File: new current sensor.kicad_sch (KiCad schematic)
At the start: 51 parts, among them J1 Conn_01x04, U1 ACS711xEXLT-31AB, U2 ACS711xEXLT-31AB, U3 ACS711xEXLT-31AB, U4 ACS711xEXLT-31AB, U5 ACS711xEXLT-31AB, U6 ACS711xEXLT-31AB, U7 ADS1119IPWR, U8 ADS1119IPWR

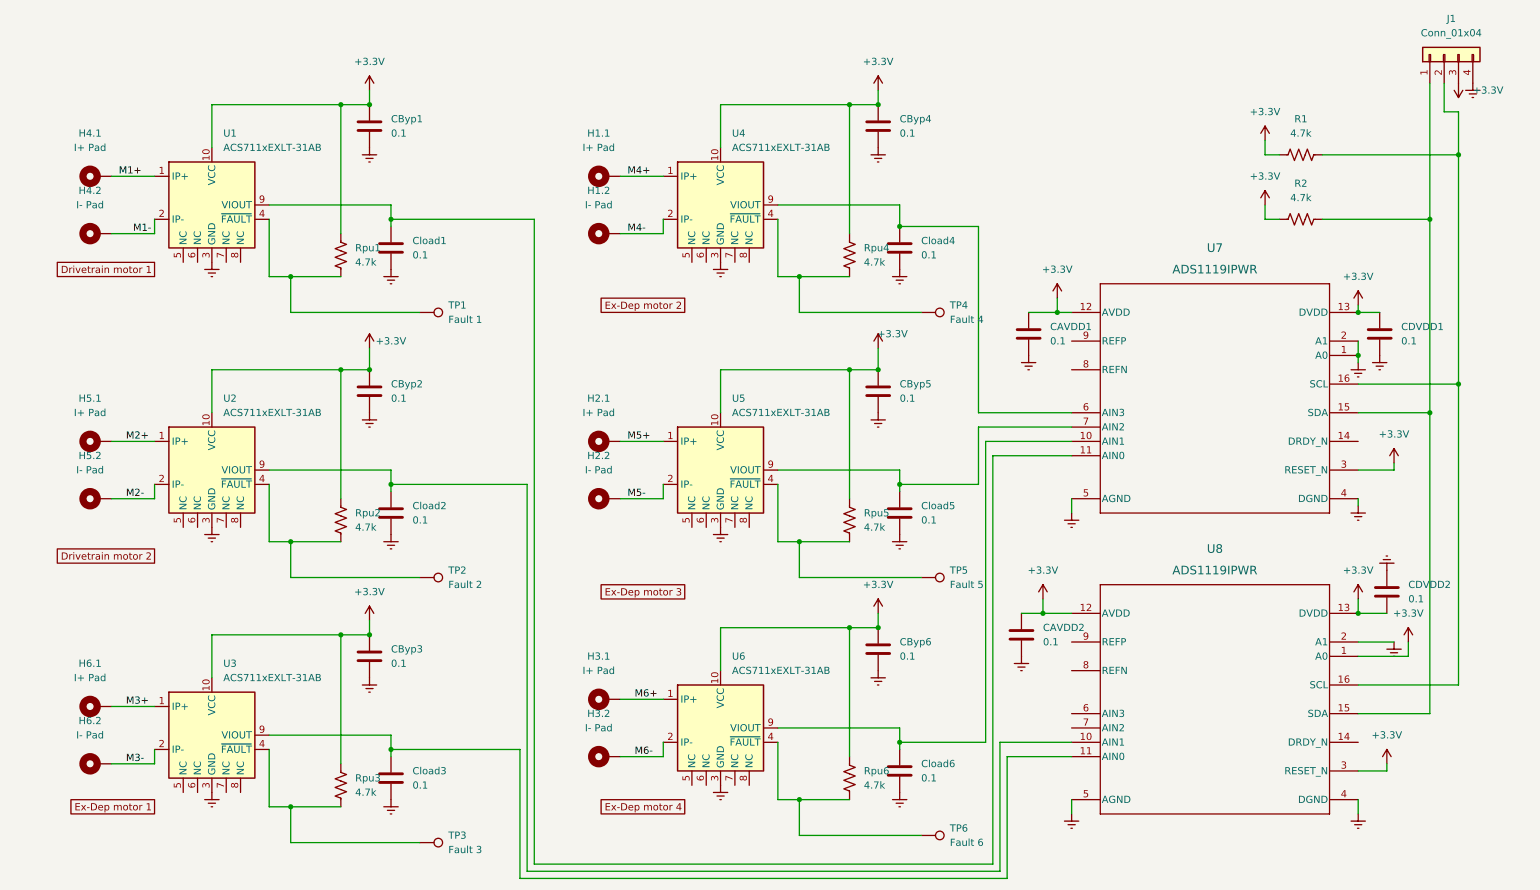
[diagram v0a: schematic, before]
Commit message: Reference pad update
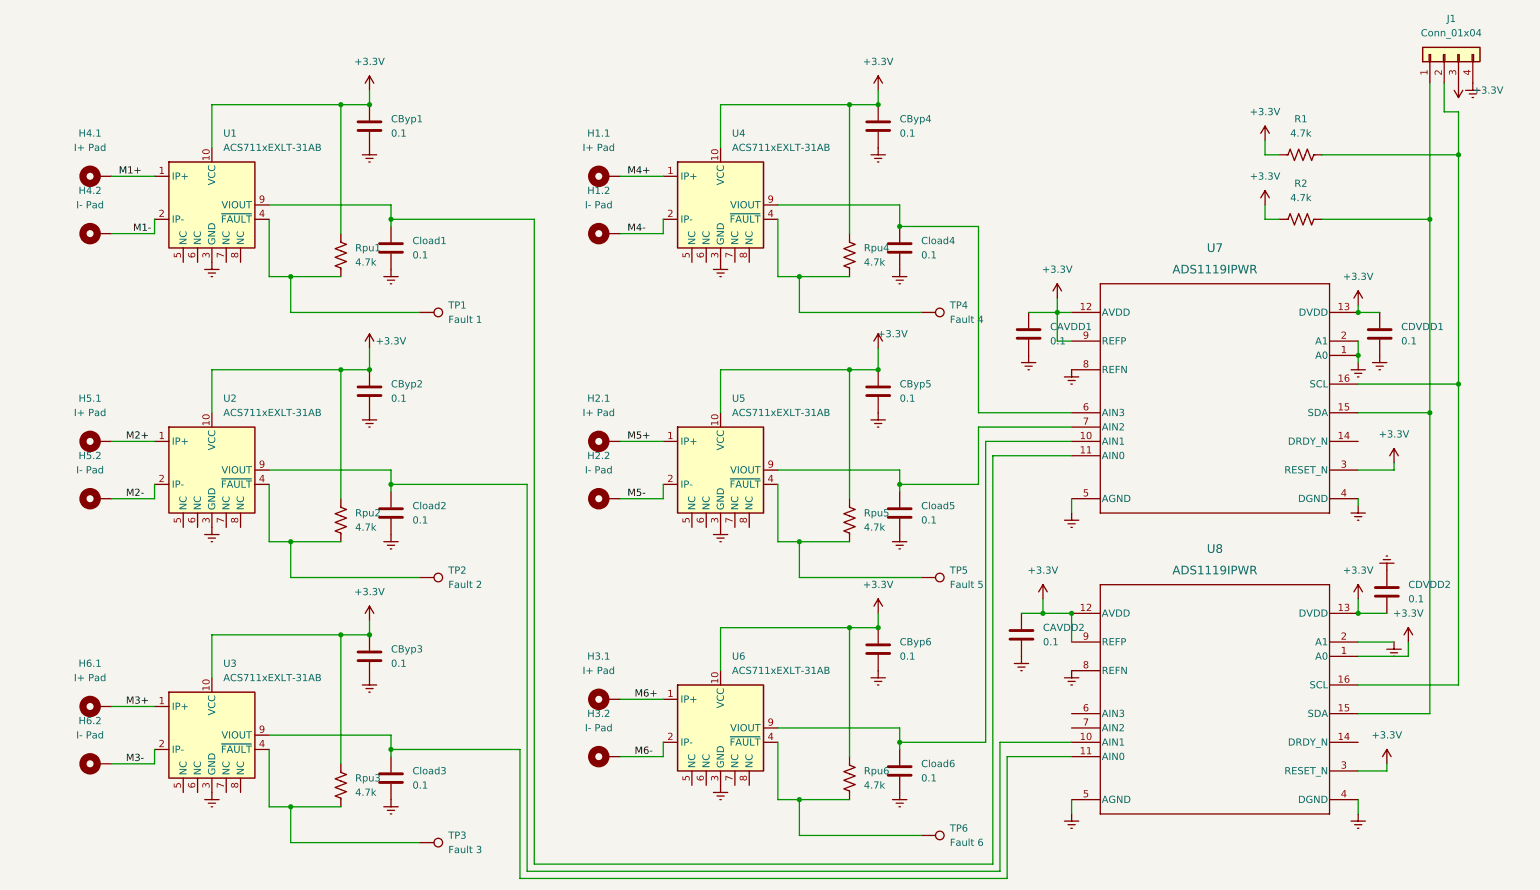
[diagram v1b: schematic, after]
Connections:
- net +3.3V: now also U7.9 (REFP), U8.9 (REFP)
- net Earth: now also U7.8 (REFN), U8.8 (REFN)
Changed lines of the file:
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@@
   (junction (at 83.82 91.44) (diameter 0) (color 0 0 0 0)
   )
+  (junction (at 204.47 114.3) (diameter 0) (color 0 0 0 0)
+  )
   (junction (at 83.82 44.45) (diameter 0) (color 0 0 0 0)
   )
@@
     (stroke (width 0) (type default) (color 0 0 0 0))
   )
+  (wire (pts (xy 204.47 66.04) (xy 201.93 66.04))
+    (stroke (width 0) (type default) (color 0 0 0 0))
+  )
   (wire (pts (xy 106.68 161.29) (xy 193.04 161.29))
     (stroke (width 0) (type default) (color 0 0 0 0))
@@
     (stroke (width 0) (type default) (color 0 0 0 0))
   )
+  (wire (pts (xy 201.93 66.04) (xy 201.93 60.96))
+    (stroke (width 0) (type default) (color 0 0 0 0))
+  )
   (wire (pts (xy 255.27 66.04) (xy 255.27 68.58))
     (stroke (width 0) (type default) (color 0 0 0 0))
@@
   )
   (wire (pts (xy 62.23 91.44) (xy 62.23 101.6))
+    (stroke (width 0) (type default) (color 0 0 0 0))
+  )
+  (wire (pts (xy 204.47 119.38) (xy 204.47 114.3))
     (stroke (width 0) (type default) (color 0 0 0 0))
   )
@@
   (label "M2-" (at 36.83 93.98 0)
     (effects (font (size 1.27 1.27)) (justify left bottom))
-  )
-  (global_label "Ex-Dep motor 4" (shape passive) (at 135.89 148.59 180) (fields_autoplaced)
-    (effects (font (size 1.27 1.27)) (justify right))
-    (property "Intersheet References" "${INTERSHEET_REFS}" (id 0) (at 117.5717 148.5106 0)
-      (effects (font (size 1.27 1.27)) (justify right) hide)
-    )
-  )
-  (global_label "Ex-Dep motor 3" (shape passive) (at 135.89 110.49 180) (fields_autoplaced)
-    (effects (font (size 1.27 1.27)) (justify right))
-    (property "Intersheet References" "${INTERSHEET_REFS}" (id 0) (at 117.5717 110.4106 0)
-      (effects (font (size 1.27 1.27)) (justify right) hide)
-    )
-  )
-  (global_label "Drivetrain motor 1" (shape passive) (at 41.91 53.34 180) (fields_autoplaced)
-    (effects (font (size 1.27 1.27)) (justify right))
-    (property "Intersheet References" "${INTERSHEET_REFS}" (id 0) (at 21.7169 53.2606 0)
-      (effects (font (size 1.27 1.27)) (justify right) hide)
-    )
-  )
-  (global_label "Ex-Dep motor 2" (shape passive) (at 135.89 59.69 180) (fields_autoplaced)
-    (effects (font (size 1.27 1.27)) (justify right))
-    (property "Intersheet References" "${INTERSHEET_REFS}" (id 0) (at 117.5717 59.6106 0)
-      (effects (font (size 1.27 1.27)) (justify right) hide)
-    )
-  )
-  (global_label "Drivetrain motor 2" (shape passive) (at 41.91 104.14 180) (fields_autoplaced)
-    (effects (font (size 1.27 1.27)) (justify right))
-    (property "Intersheet References" "${INTERSHEET_REFS}" (id 0) (at 21.7169 104.0606 0)
-      (effects (font (size 1.27 1.27)) (justify right) hide)
-    )
-  )
-  (global_label "Ex-Dep motor 1" (shape passive) (at 41.91 148.59 180) (fields_autoplaced)
-    (effects (font (size 1.27 1.27)) (justify right))
-    (property "Intersheet References" "${INTERSHEET_REFS}" (id 0) (at 23.5917 148.5106 0)
-      (effects (font (size 1.27 1.27)) (justify right) hide)
-    )
   )
   (symbol (lib_id "Sensor_Current:ACS711xEXLT-31AB") (at 52.07 88.9 0) (unit 1)
@@
     (pin "2")
   )
+  (symbol (lib_id "power:Earth") (at 204.47 124.46 0) (unit 1)
+    (in_bom yes) (on_board yes) (fields_autoplaced)
+    (property "Reference" "#PWR?" (id 0) (at 204.47 130.81 0)
+      (effects (font (size 1.27 1.27)) hide)
+    )
+    (property "Value" "Earth" (id 1) (at 204.47 128.27 0)
+      (effects (font (size 1.27 1.27)) hide)
+    )
+    (property "Footprint" "" (id 2) (at 204.47 124.46 0)
+      (effects (font (size 1.27 1.27)) hide)
+    )
+    (property "Datasheet" "~" (id 3) (at 204.47 124.46 0)
+      (effects (font (size 1.27 1.27)) hide)
+    )
+    (pin "1")
+  )
   (symbol (lib_id "Device:C") (at 170.18 74.93 0) (unit 1)
     (in_bom yes) (on_board yes) (fields_autoplaced)
@@
     (pin "1")
   )
+  (symbol (lib_id "power:Earth") (at 204.47 71.12 0) (unit 1)
+    (in_bom yes) (on_board yes) (fields_autoplaced)
+    (property "Reference" "#PWR?" (id 0) (at 204.47 77.47 0)
+      (effects (font (size 1.27 1.27)) hide)
+    )
+    (property "Value" "Earth" (id 1) (at 204.47 74.93 0)
+      (effects (font (size 1.27 1.27)) hide)
+    )
+    (property "Footprint" "" (id 2) (at 204.47 71.12 0)
+      (effects (font (size 1.27 1.27)) hide)
+    )
+    (property "Datasheet" "~" (id 3) (at 204.47 71.12 0)
+      (effects (font (size 1.27 1.27)) hide)
+    )
+    (pin "1")
+  )
   (symbol (lib_id "Device:R_US") (at 245.11 33.02 90) (unit 1)
     (in_bom yes) (on_board yes) (fields_autoplaced)
@@
       (reference "#PWR0145") (unit 1) (value "Earth") (footprint "")
     )
+    (path "/98e7eeb4-97b5-4e45-8aaa-ba7ec1962685"
+      (reference "#PWR?") (unit 1) (value "Earth") (footprint "")
+    )
+    (path "/e8b5215e-6249-4fe8-a99d-223dc179da16"
+      (reference "#PWR?") (unit 1) (value "Earth") (footprint "")
+    )
     (path "/d4b627a4-02a7-44ad-947c-71e3508a29ed"

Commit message: midway point
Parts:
- added CAVDDRP1, CAVDDRP2: 0.1, Capacitor_SMD:C_0805_2012Metric_Pad1.18x1.45mm_HandSolder, symbol Device:C
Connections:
- net +3.3V: now also CAVDDRP1.1, CAVDDRP2.1
- net Earth: now also CAVDDRP1.2, CAVDDRP2.2
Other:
- moved on the sheet: CAVDD1

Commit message: final changes
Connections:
- no-connect marks 0 -> 24

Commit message: final changes
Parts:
- added TP10: 3.3V, Connector_Wire:SolderWire-0.1sqmm_1x01_D0.4mm_OD1mm, symbol Connector:TestPoint
- added TP7: SCL, Connector_Wire:SolderWire-0.1sqmm_1x01_D0.4mm_OD1mm, symbol Connector:TestPoint
- added TP8: SDA, Connector_Wire:SolderWire-0.1sqmm_1x01_D0.4mm_OD1mm, symbol Connector:TestPoint
- added TP9: GND, Connector_Wire:SolderWire-0.1sqmm_1x01_D0.4mm_OD1mm, symbol Connector:TestPoint
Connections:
- net +3V3 is gone; now on net +3.3V: J1.3 (Pin_3)
- net +3.3V: now also TP10.1
- net Earth: now also TP9.1
- net SDA: now reaches J1.1 (Pin_1), R2.2, U7.15 (SDA), U8.15 (SDA)
- net SDA: now also TP8.1
- net SCL: now reaches J1.2 (Pin_2), R1.2, U7.16 (SCL), U8.16 (SCL)
- net SCL: now also TP7.1
